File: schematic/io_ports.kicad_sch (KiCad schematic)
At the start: 3 parts, among them J1 Cartridge Port, J2 Expansion Port

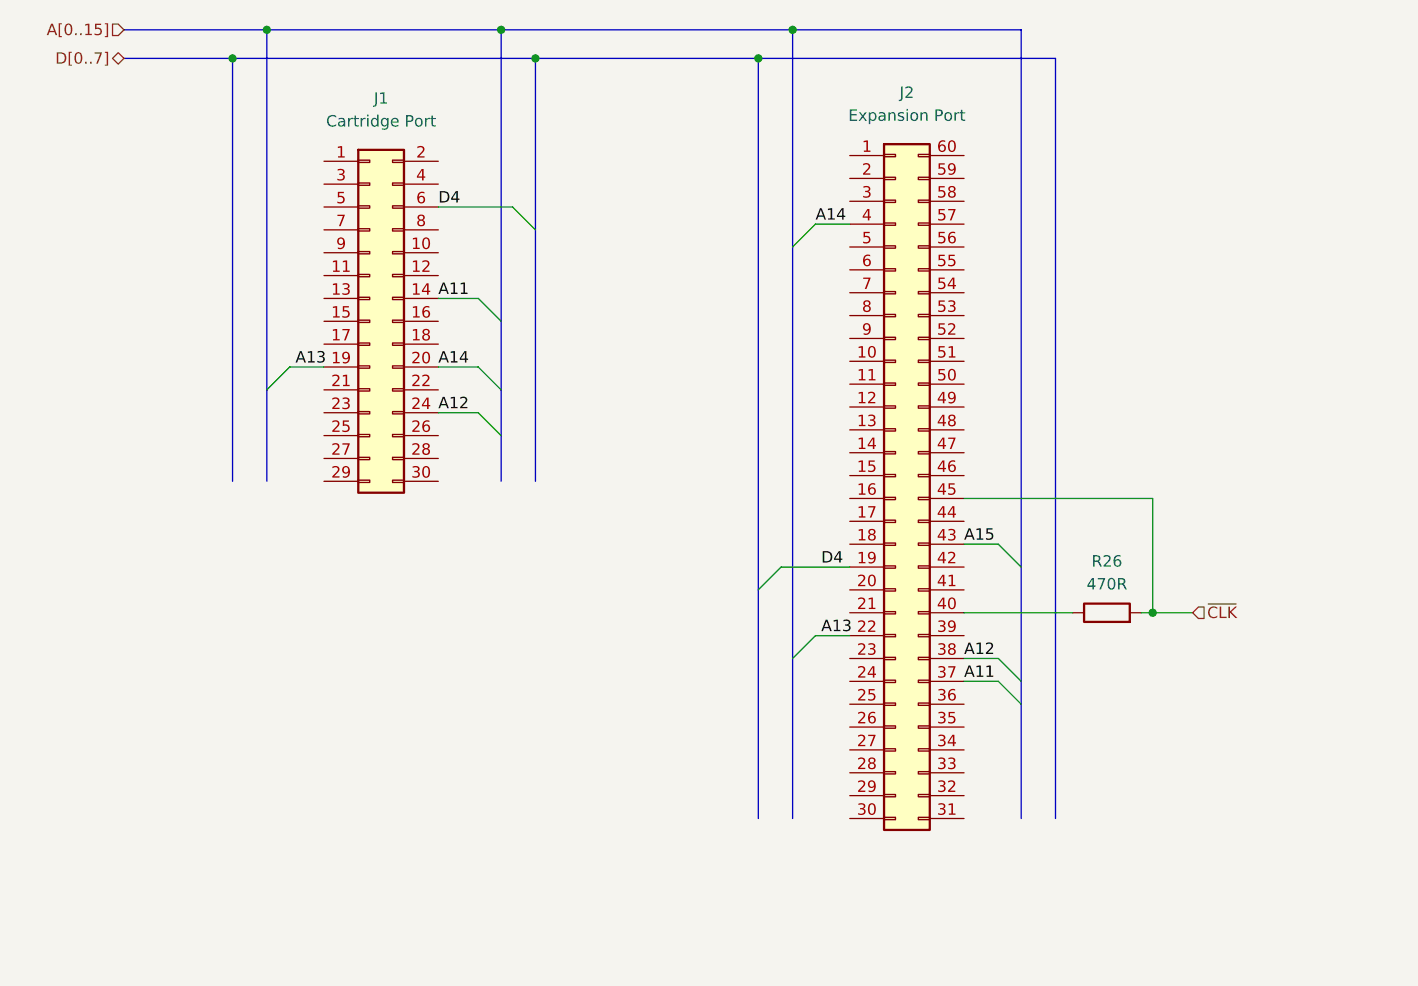
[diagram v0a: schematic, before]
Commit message: worked on the z80 trace up to and including pin 15.
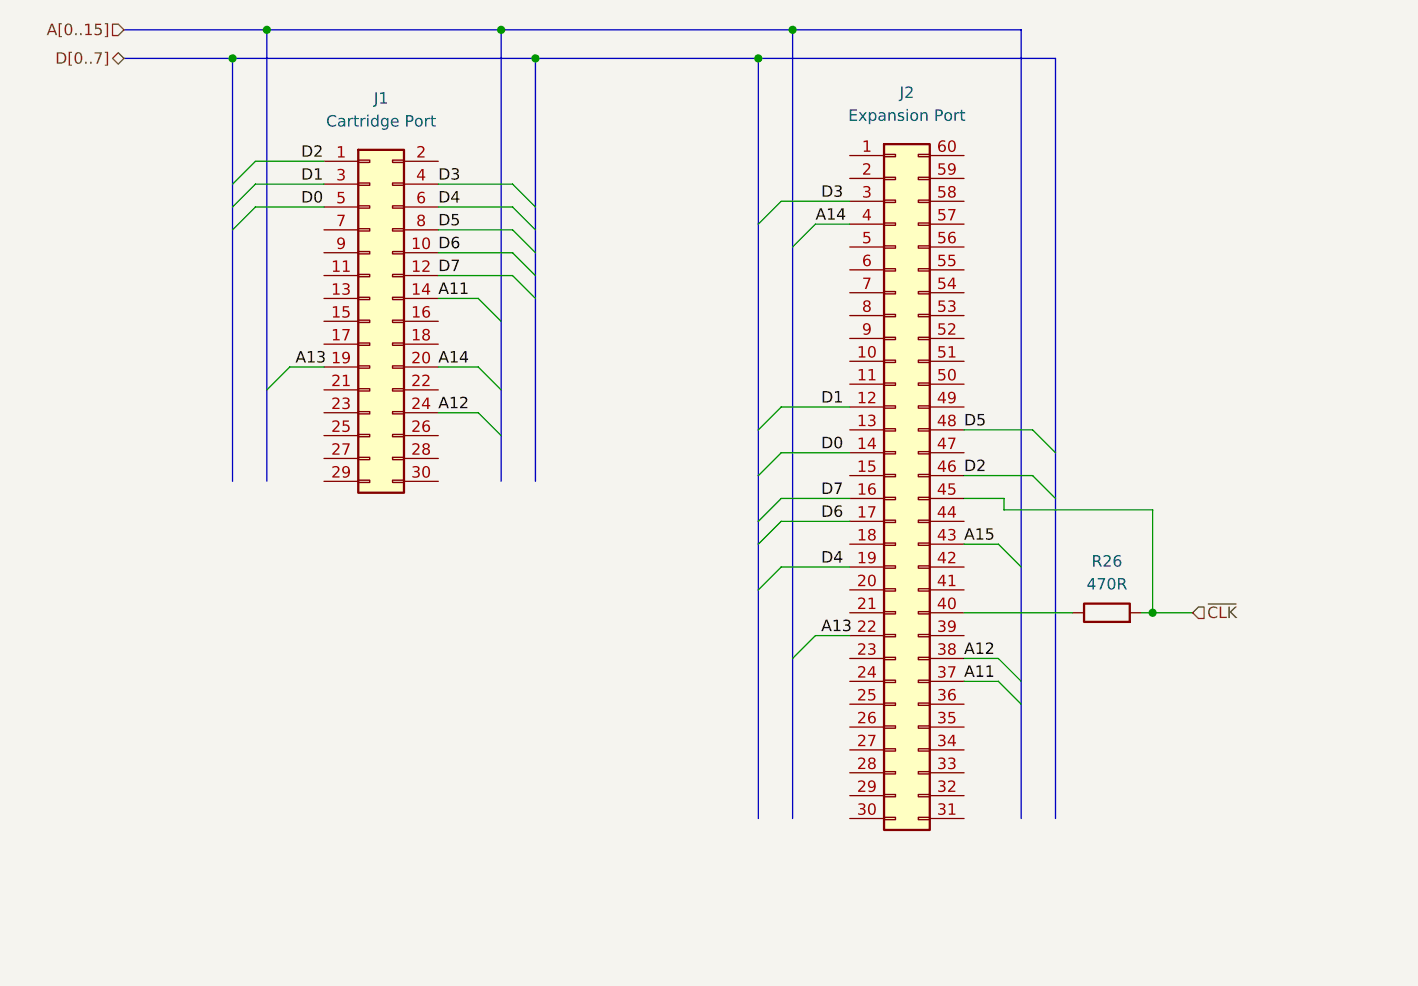
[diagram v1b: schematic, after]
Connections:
- net D2: now reaches J1.1 (Pin_1)
- net D2: now also J2.46 (Pin_46)
- net D6: now reaches J1.10 (Pin_10)
- net D6: now also J2.17 (Pin_17)
- net D7: now reaches J1.12 (Pin_12)
- net D7: now also J2.16 (Pin_16)
- net D1: now reaches J1.3 (Pin_3)
- net D1: now also J2.12 (Pin_12)
- net D3: now reaches J1.4 (Pin_4)
- net D3: now also J2.3 (Pin_3)
- net D0: now reaches J1.5 (Pin_5)
- net D0: now also J2.14 (Pin_14)
- net D5: now reaches J1.8 (Pin_8)
- net D5: now also J2.48 (Pin_48)

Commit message: Up to pin 29 on z80 done. Address 0 to 10 left. Only tracing to its end point for the most part. Each chip gets traced chip to chip in this manned
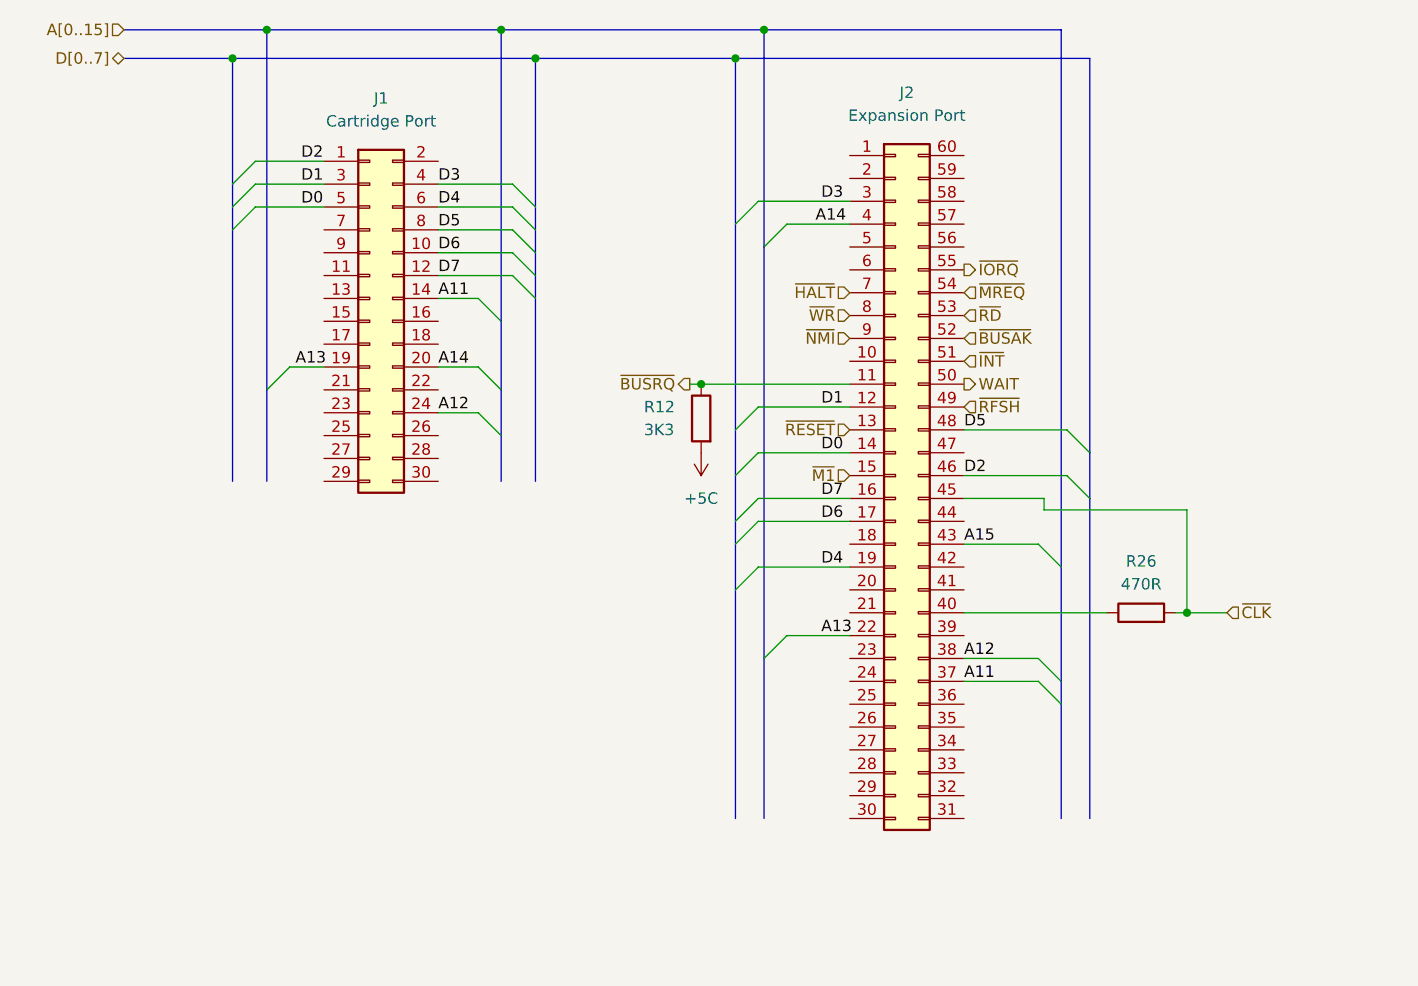
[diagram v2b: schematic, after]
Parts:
- added R12: 3K3, symbol Device:R
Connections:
- net ~{BUSRQ}: now reaches J2.11 (Pin_11)
- net ~{BUSRQ}: now also R12.1
- net ~{RESET}: now reaches J2.13 (Pin_13)
- net ~{M1}: now reaches J2.15 (Pin_15)
- net ~{RFSH}: now reaches J2.49 (Pin_49)
- net WAIT: now reaches J2.50 (Pin_50)
- net ~{INT}: now reaches J2.51 (Pin_51)
- net ~{BUSAK}: now reaches J2.52 (Pin_52)
- net ~{RD}: now reaches J2.53 (Pin_53)
- net ~{MREQ}: now reaches J2.54 (Pin_54)
- net ~{IORQ}: now reaches J2.55 (Pin_55)
- net ~{HALT}: now reaches J2.7 (Pin_7)
- net ~{WR}: now reaches J2.8 (Pin_8)
- net ~{NMI}: now reaches J2.9 (Pin_9)
- new net +5C: R12.2
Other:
- moved on the sheet: R26

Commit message: completed Z80 trace of PCB. off to a good start.
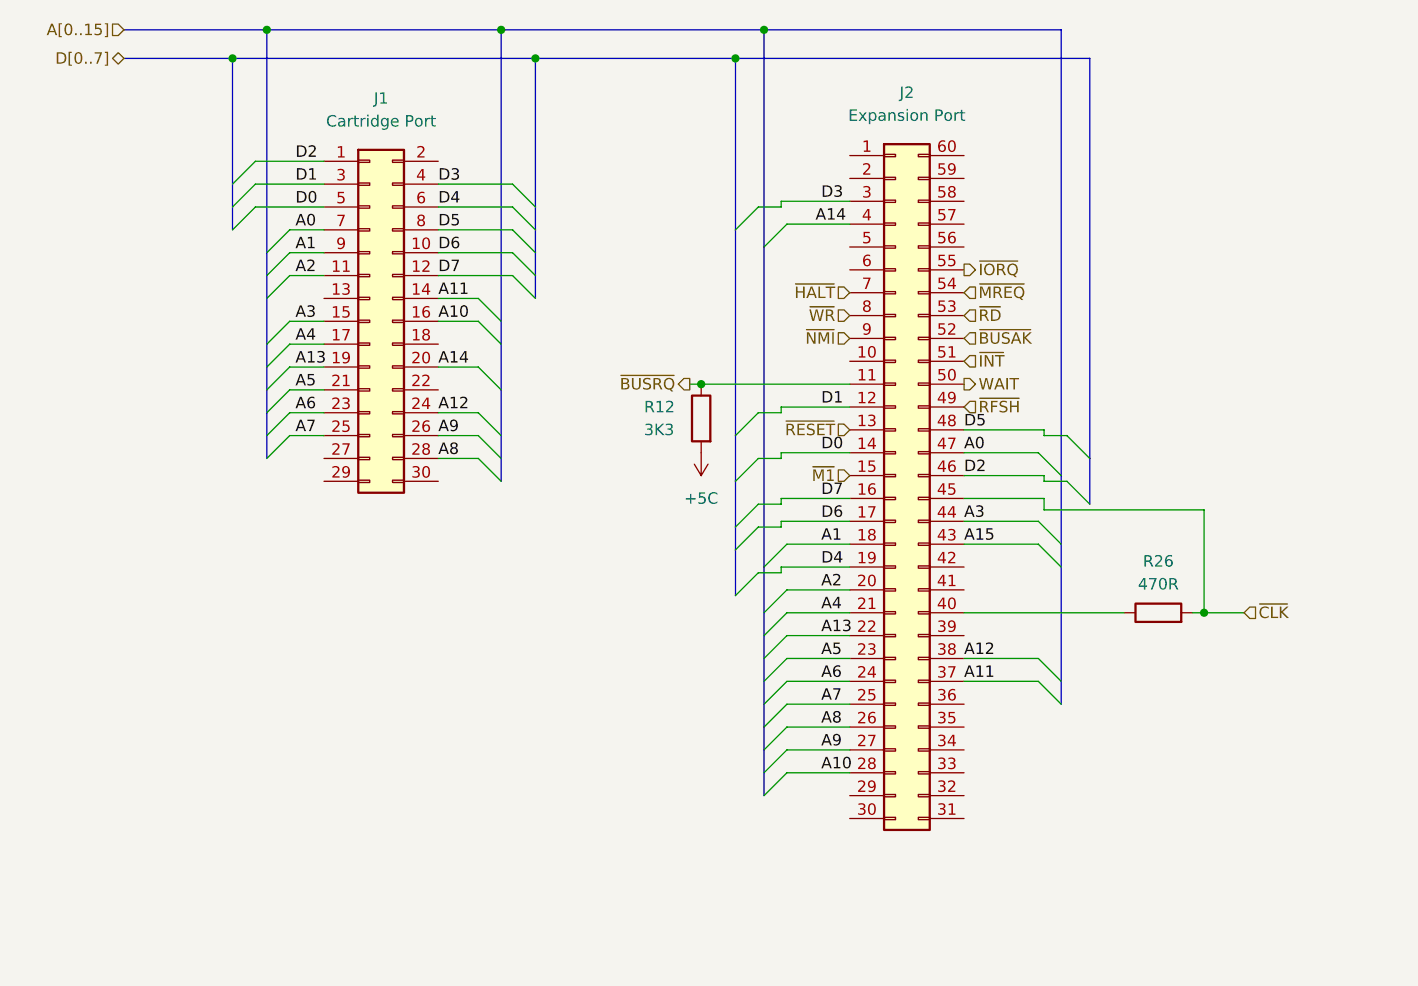
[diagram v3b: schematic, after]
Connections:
- net A2: now reaches J1.11 (Pin_11)
- net A2: now also J2.20 (Pin_20)
- net A3: now reaches J1.15 (Pin_15)
- net A3: now also J2.44 (Pin_44)
- net A10: now reaches J1.16 (Pin_16)
- net A10: now also J2.28 (Pin_28)
- net A4: now reaches J1.17 (Pin_17)
- net A4: now also J2.21 (Pin_21)
- net A5: now reaches J1.21 (Pin_21)
- net A5: now also J2.23 (Pin_23)
- net A6: now reaches J1.23 (Pin_23)
- net A6: now also J2.24 (Pin_24)
- net A7: now reaches J1.25 (Pin_25)
- net A7: now also J2.25 (Pin_25)
- net A9: now reaches J1.26 (Pin_26)
- net A9: now also J2.27 (Pin_27)
- net A8: now reaches J1.28 (Pin_28)
- net A8: now also J2.26 (Pin_26)
- net A0: now reaches J1.7 (Pin_7)
- net A0: now also J2.47 (Pin_47)
- net A1: now reaches J1.9 (Pin_9)
- net A1: now also J2.18 (Pin_18)
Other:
- moved on the sheet: R26

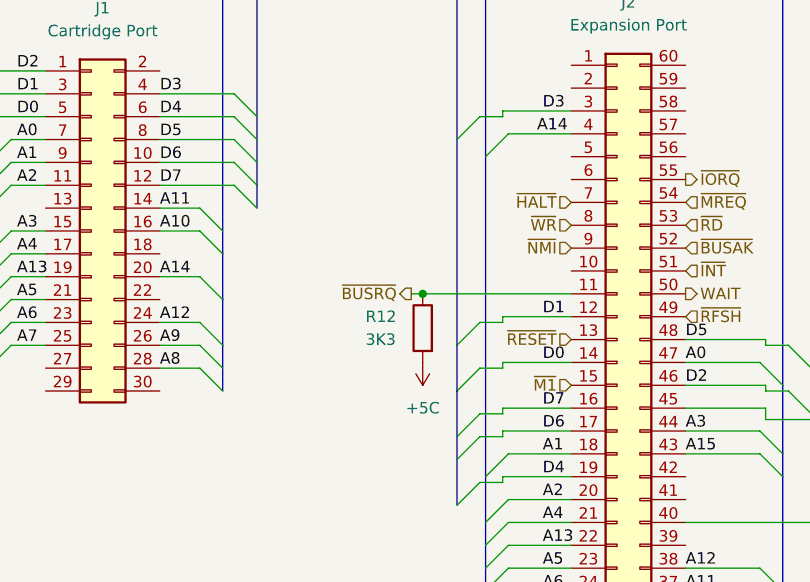
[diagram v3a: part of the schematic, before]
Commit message: added rf modulation schematic, added dram to vdp. Fixed +5vc to +5v
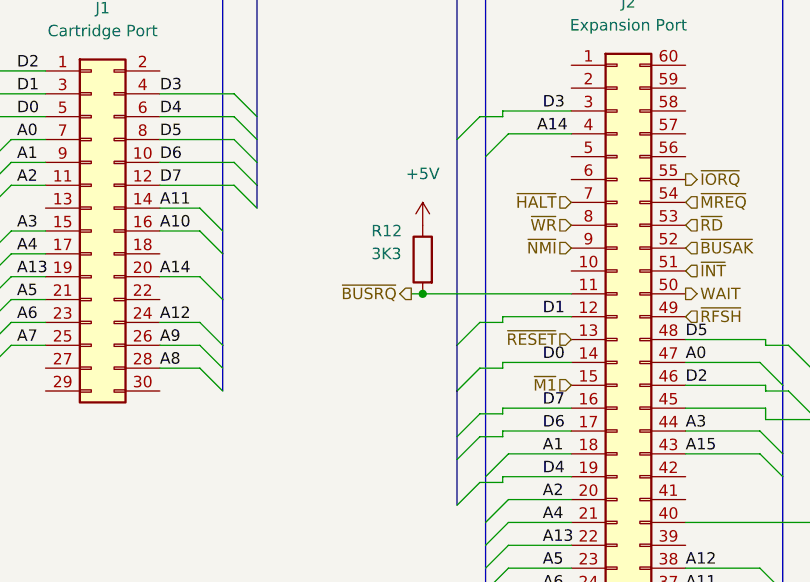
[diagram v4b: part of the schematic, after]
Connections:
- net +5C is gone; now on net ~{BUSRQ}: R12.2
- net ~{BUSRQ}: no longer R12.1
- new net +5V: R12.1
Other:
- moved on the sheet: R12
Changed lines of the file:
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@@
   (junction (at 153.67 33.02) (diameter 0) (color 0 0 0 0)
   )
+  (junction (at 146.685 72.39) (diameter 0) (color 0 0 0 0)
+  )
   (junction (at 94.615 36.195) (diameter 0) (color 0 0 0 0)
   )
@@
   (junction (at 124.46 33.02) (diameter 0) (color 0 0 0 0)
   )
-  (junction (at 146.685 72.39) (diameter 0) (color 0 0 0 0)
-  )
   (junction (at 128.27 36.195) (diameter 0) (color 0 0 0 0)
   )
@@
     (stroke (width 0) (type default) (color 0 0 0 0))
   )
+  (wire (pts (xy 146.685 72.39) (xy 163.195 72.39))
+    (stroke (width 0) (type default) (color 0 0 0 0))
+  )
   (wire (pts (xy 153.035 75.565) (xy 155.575 75.565))
     (stroke (width 0) (type default) (color 0 0 0 0))
@@
     (stroke (width 0) (type default) (color 0 0 0 0))
   )
-  (wire (pts (xy 146.685 72.39) (xy 163.195 72.39))
+  (wire (pts (xy 145.415 72.39) (xy 146.685 72.39))
     (stroke (width 0) (type default) (color 0 0 0 0))
   )
@@
   )
   (bus (pts (xy 153.67 107.95) (xy 153.67 110.49))
-    (stroke (width 0) (type default) (color 0 0 0 0))
-  )
-  (wire (pts (xy 145.415 72.39) (xy 146.685 72.39))
     (stroke (width 0) (type default) (color 0 0 0 0))
   )
@@
     (pin "1")
     (pin "2")
-  )
-  (symbol (lib_id "power:+5C") (at 146.685 80.01 180) (unit 1)
-    (in_bom yes) (on_board yes) (fields_autoplaced)
-    (property "Reference" "#PWR?" (id 0) (at 146.685 76.2 0)
-      (effects (font (size 1.27 1.27)) hide)
-    )
-    (property "Value" "+5C" (id 1) (at 146.685 85.09 0))
-    (property "Footprint" "" (id 2) (at 146.685 80.01 0)
-      (effects (font (size 1.27 1.27)) hide)
-    )
-    (property "Datasheet" "" (id 3) (at 146.685 80.01 0)
-      (effects (font (size 1.27 1.27)) hide)
-    )
-    (pin "1")
   )
   (symbol (lib_id "Connector_Generic:Conn_02x30_Counter_Clockwise") (at 168.275 82.55 0) (unit 1)
@@
     (pin "9")
   )
-  (symbol (lib_id "Device:R") (at 146.685 76.2 0) (mirror y) (unit 1)
+  (symbol (lib_id "power:+5V") (at 146.685 64.77 0) (unit 1)
+    (in_bom yes) (on_board yes) (fields_autoplaced)
+    (property "Reference" "#PWR?" (id 0) (at 146.685 68.58 0)
+      (effects (font (size 1.27 1.27)) hide)
+    )
+    (property "Value" "+5V" (id 1) (at 146.685 59.055 0))
+    (property "Footprint" "" (id 2) (at 146.685 64.77 0)
+      (effects (font (size 1.27 1.27)) hide)
+    )
+    (property "Datasheet" "" (id 3) (at 146.685 64.77 0)
+      (effects (font (size 1.27 1.27)) hide)
+    )
+    (pin "1")
+  )
+  (symbol (lib_id "Device:R") (at 146.685 68.58 0) (mirror y) (unit 1)
     (in_bom yes) (on_board yes)
-    (property "Reference" "R12" (id 0) (at 140.335 74.93 0)
+    (property "Reference" "R12" (id 0) (at 140.97 65.405 0)
       (effects (font (size 1.27 1.27)) (justify right))
     )
-    (property "Value" "3K3" (id 1) (at 140.335 77.47 0)
+    (property "Value" "3K3" (id 1) (at 140.97 67.945 0)
       (effects (font (size 1.27 1.27)) (justify right))
     )
-    (property "Footprint" "" (id 2) (at 148.463 76.2 90)
-      (effects (font (size 1.27 1.27)) hide)
-    )
-    (property "Datasheet" "~" (id 3) (at 146.685 76.2 0)
-      (effects (font (size 1.27 1.27)) hide)
-    )
+    (property "Footprint" "" (id 2) (at 148.463 68.58 90)
+      (effects (font (size 1.27 1.27)) hide)
+    )
+    (property "Datasheet" "~" (id 3) (at 146.685 68.58 0)
+      (effects (font (size 1.27 1.27)) hide)
+    )
